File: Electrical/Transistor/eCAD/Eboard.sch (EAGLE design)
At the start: 22 parts

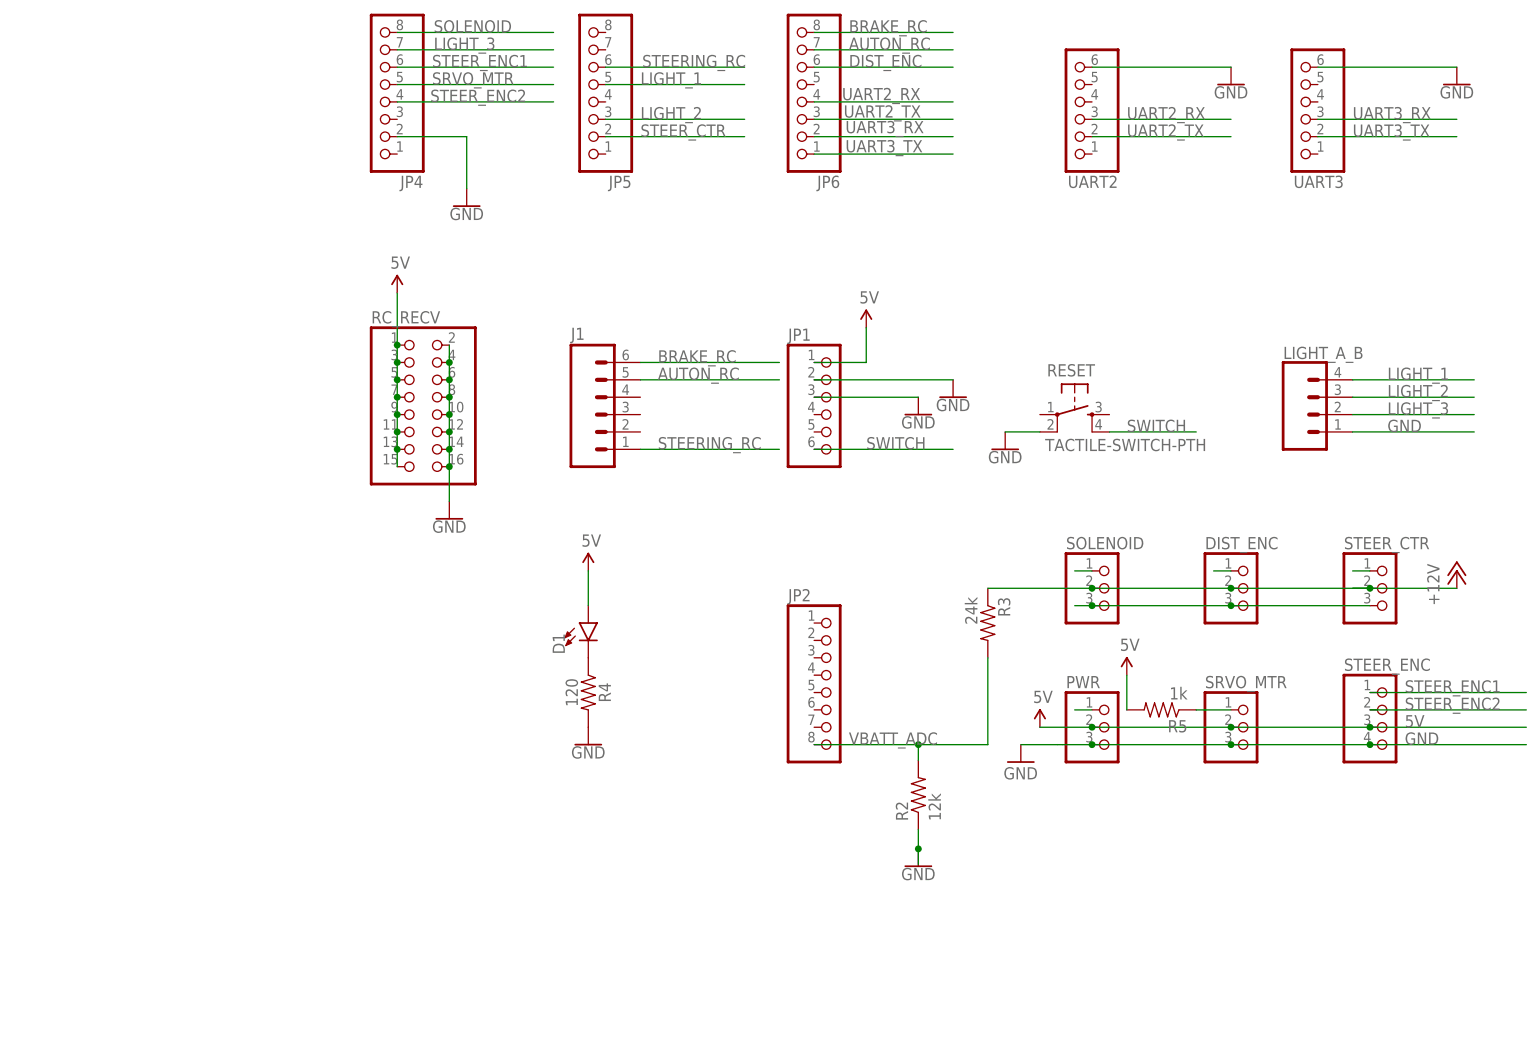
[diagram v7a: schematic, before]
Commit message: reversed steering pins to match configuration of existing connector
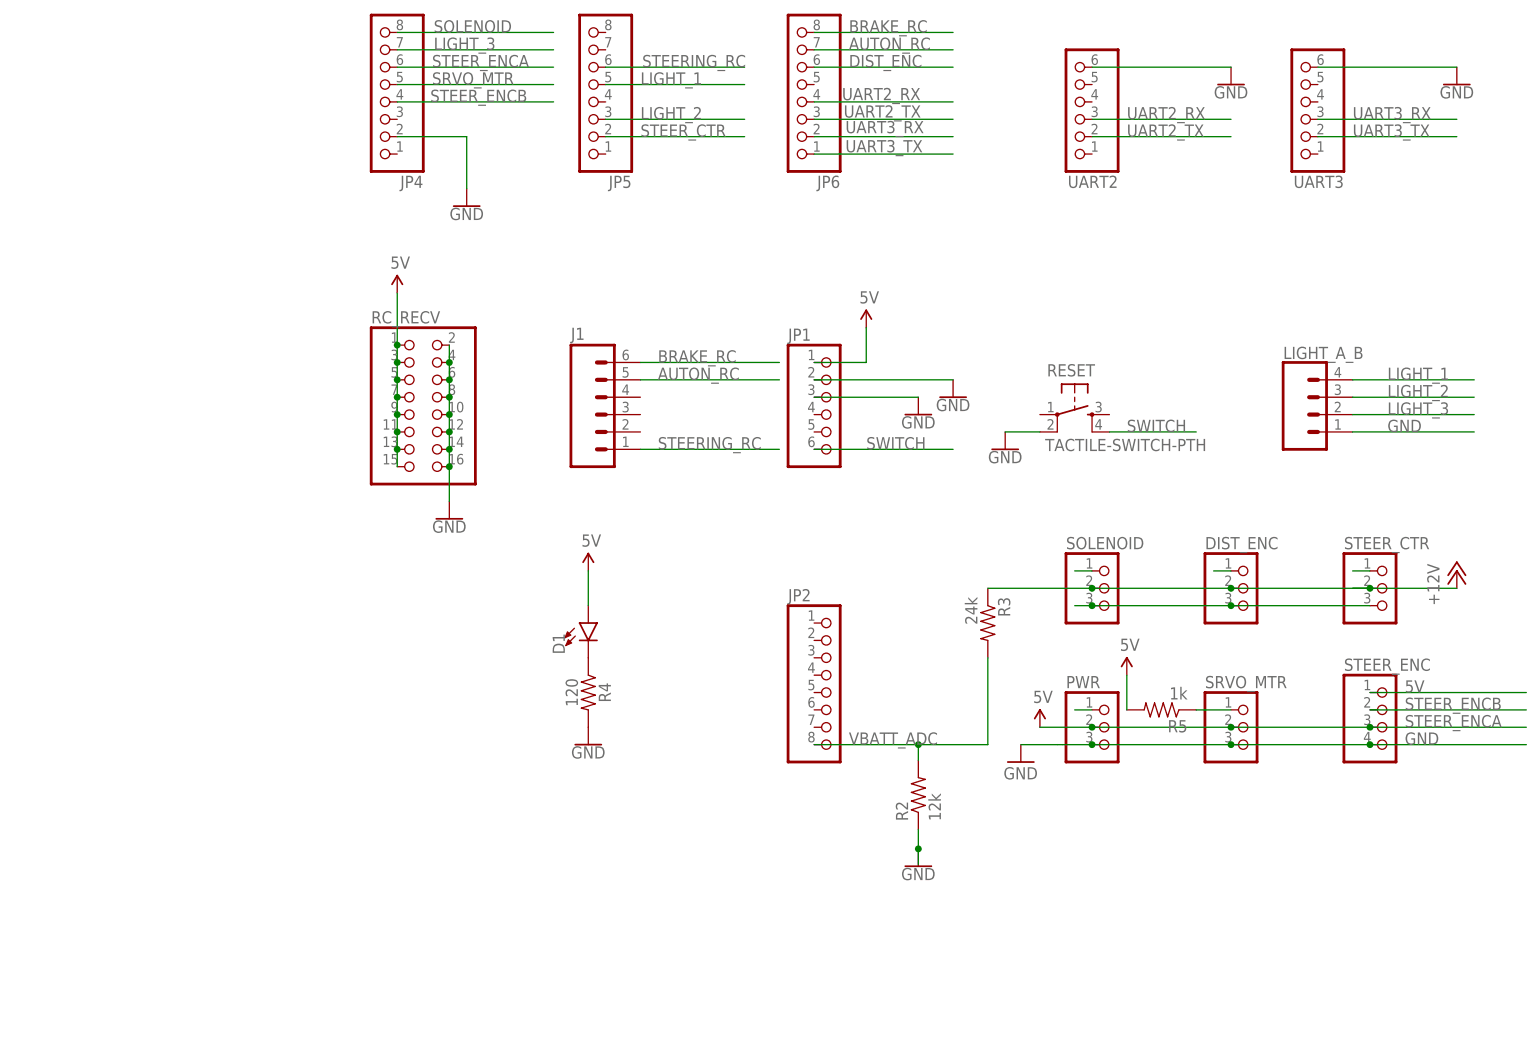
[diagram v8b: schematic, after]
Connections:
- net STEER_ENC2 renamed STEER_ENCB
- removed net STEER_ENC1: JP4.6, STEER_ENC.1
- new net STEER_ENCA: JP4.6, PWR.2, SRVO_MTR.2, STEER_ENC.3
- net 5V: now also STEER_ENC.1; no longer PWR.2, SRVO_MTR.2, STEER_ENC.3
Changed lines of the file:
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@@
-</segment>
-<segment>
-<pinref part="PWR" gate="A" pin="2"/>
-<pinref part="SRVO_MTR" gate="A" pin="2"/>
-<wire x1="160.02" y1="76.2" x2="180.34" y2="76.2" width="0.1524" layer="91"/>
-<junction x="180.34" y="76.2"/>
-<pinref part="STEER_ENC" gate="A" pin="3"/>
-<label x="205.74" y="76.2" size="1.778" layer="95"/>
-<wire x1="200.66" y1="76.2" x2="223.52" y2="76.2" width="0.1524" layer="91"/>
-<junction x="200.66" y="76.2"/>
-<wire x1="180.34" y1="76.2" x2="200.66" y2="76.2" width="0.1524" layer="91"/>
-<pinref part="SUPPLY1" gate="G$1" pin="5V"/>
-<wire x1="152.4" y1="76.2" x2="160.02" y2="76.2" width="0.1524" layer="91"/>
-<junction x="160.02" y="76.2"/>
 </segment>
 <segment>
@@
 <wire x1="127" y1="129.54" x2="127" y2="134.62" width="0.1524" layer="91"/>
 <pinref part="SUPPLY5" gate="G$1" pin="5V"/>
+</segment>
+<segment>
+<pinref part="STEER_ENC" gate="A" pin="1"/>
+<label x="205.74" y="81.28" size="1.778" layer="95"/>
+<wire x1="200.66" y1="81.28" x2="223.52" y2="81.28" width="0.1524" layer="91"/>
 </segment>
 </net>
@@
 </segment>
 </net>
-<net name="STEER_ENC1" class="0">
-<segment>
-<pinref part="STEER_ENC" gate="A" pin="1"/>
-<label x="205.74" y="81.28" size="1.778" layer="95"/>
-<wire x1="200.66" y1="81.28" x2="223.52" y2="81.28" width="0.1524" layer="91"/>
-</segment>
+<net name="STEER_ENCA" class="0">
 <segment>
 <pinref part="JP4" gate="A" pin="6"/>
@@
 <wire x1="58.42" y1="172.72" x2="81.28" y2="172.72" width="0.1524" layer="91"/>
 </segment>
-</net>
-<net name="STEER_ENC2" class="0">
+<segment>
+<pinref part="PWR" gate="A" pin="2"/>
+<pinref part="SRVO_MTR" gate="A" pin="2"/>
+<wire x1="160.02" y1="76.2" x2="180.34" y2="76.2" width="0.1524" layer="91"/>
+<junction x="180.34" y="76.2"/>
+<pinref part="STEER_ENC" gate="A" pin="3"/>
+<label x="205.74" y="76.2" size="1.778" layer="95"/>
+<wire x1="200.66" y1="76.2" x2="223.52" y2="76.2" width="0.1524" layer="91"/>
+<junction x="200.66" y="76.2"/>
+<wire x1="180.34" y1="76.2" x2="200.66" y2="76.2" width="0.1524" layer="91"/>
+<pinref part="SUPPLY1" gate="G$1" pin="5V"/>
+<wire x1="152.4" y1="76.2" x2="160.02" y2="76.2" width="0.1524" layer="91"/>
+<junction x="160.02" y="76.2"/>
+</segment>
+</net>
+<net name="STEER_ENCB" class="0">
 <segment>
 <pinref part="STEER_ENC" gate="A" pin="2"/>
